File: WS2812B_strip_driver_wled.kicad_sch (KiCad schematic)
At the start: 114 parts, among them J1 CH_1, J2 CH_2, J3 CH_3, J4 CH_4, J5 PWR_IN, J6 uPhone, J8 USB_C_Receptacle_USB2.0_16P, K1 RELAY_1, K2 RELAY_2, K3 RELAY_3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

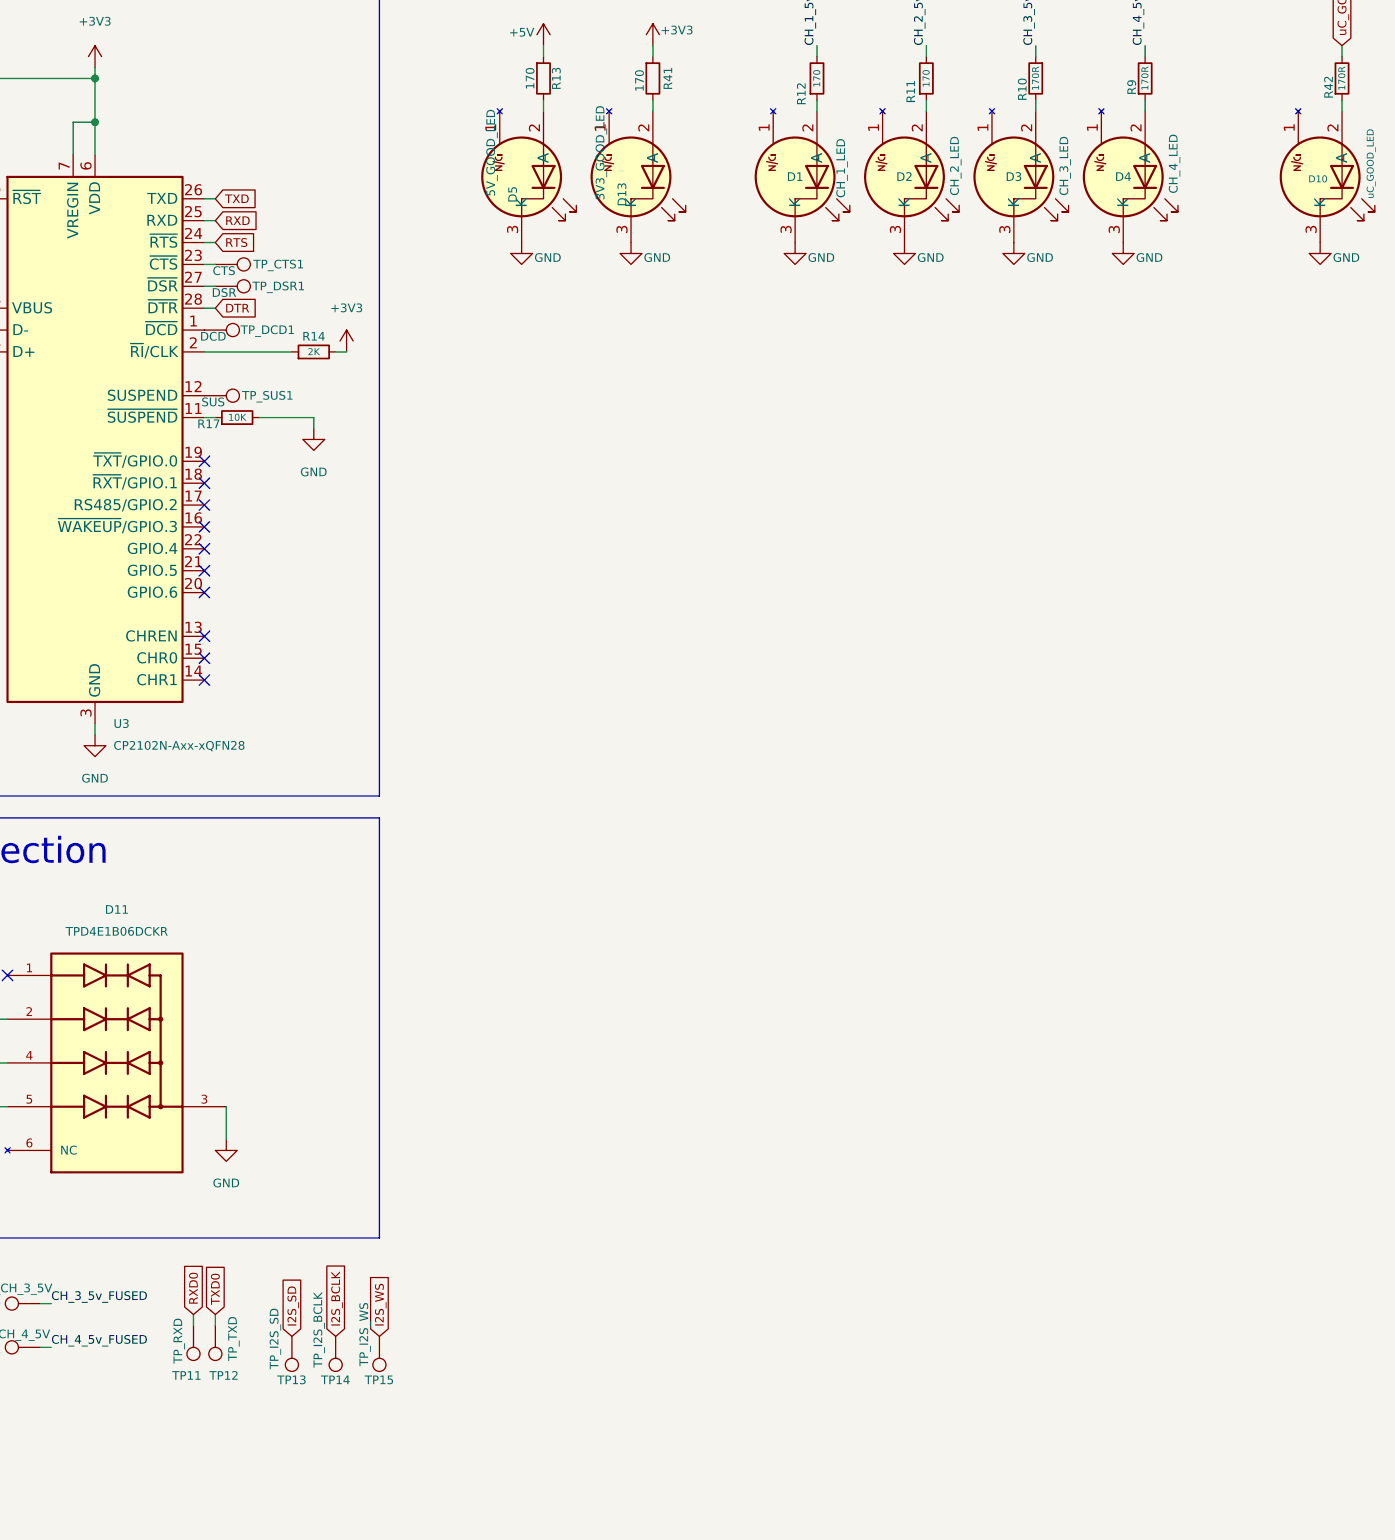
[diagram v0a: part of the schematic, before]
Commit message: More silkscreen improvements/additions
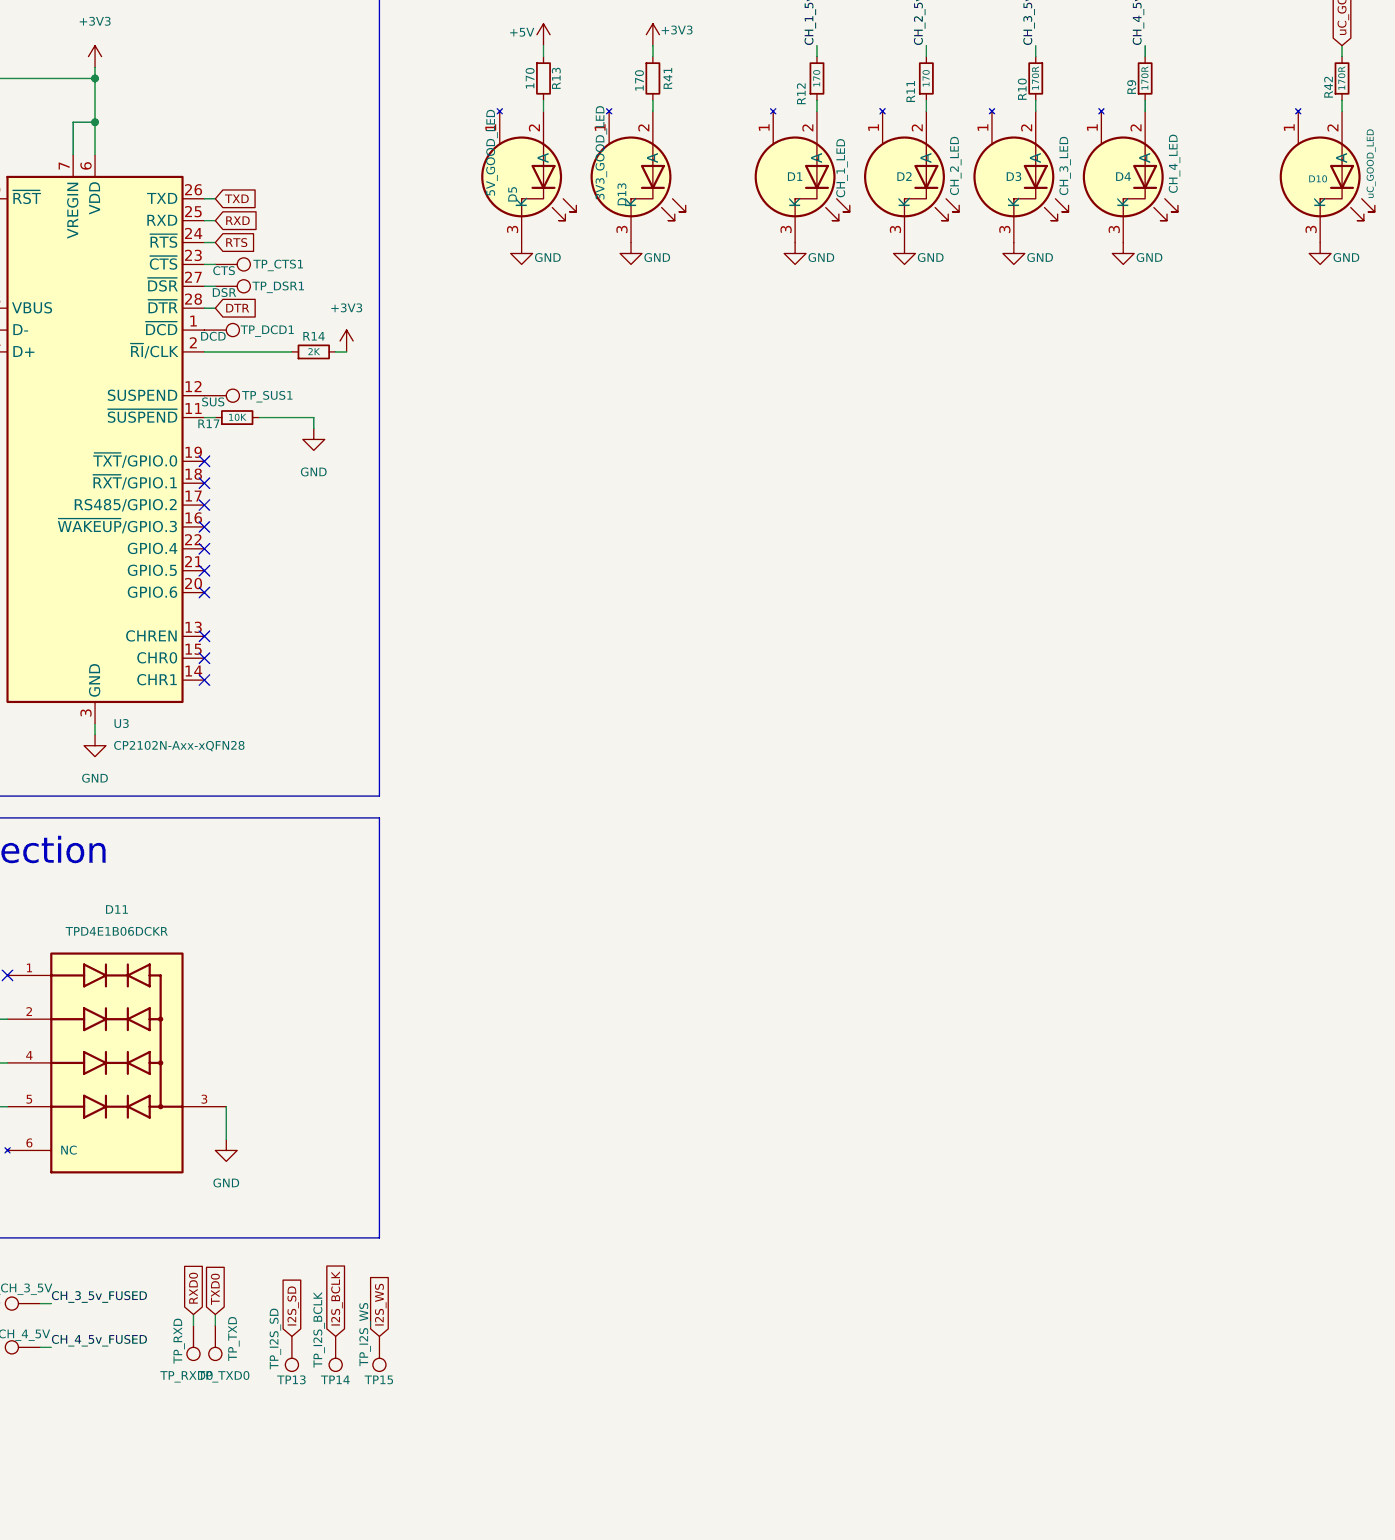
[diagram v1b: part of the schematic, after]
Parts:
- renumbered TP11 to TP_RXD0, TP12 to TP_TXD0
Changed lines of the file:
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@@
 			)
 		)
-		(property "Description" "Light emitting diode, small symbol, filled shape"
-			(at 331.47 40.64 0)
-			(effects
-				(font
-					(size 1.27 1.27)
-				)
-				(hide yes)
-			)
-		)
-		(property "Sim.Pins" "1=K 2=A"
+		(property "Description" ""
 			(at 331.47 40.64 0)
 			(effects
@@
 			)
 		)
-		(property "Description" "Light emitting diode, small symbol, filled shape"
-			(at 392.43 40.64 0)
-			(effects
-				(font
-					(size 1.27 1.27)
-				)
-				(hide yes)
-			)
-		)
-		(property "Sim.Pins" "1=K 2=A"
+		(property "Description" ""
 			(at 392.43 40.64 0)
 			(effects
@@
 		(on_board yes)
 		(dnp no)
-		(property "Reference" "TP12"
+		(property "Reference" "TP_TXD0"
 			(at 265.176 179.832 0)
 			(effects
@@
 			(project "WS2812B_strip_driver_wled"
 				(path "/a67e84d5-b812-4302-b0a6-200741099847"
-					(reference "TP12")
+					(reference "TP_TXD0")
 					(unit 1)
 				)
@@
 			)
 		)
-		(property "Description" "Light emitting diode, small symbol, filled shape"
-			(at 356.87 40.64 0)
-			(effects
-				(font
-					(size 1.27 1.27)
-				)
-				(hide yes)
-			)
-		)
-		(property "Sim.Pins" "1=K 2=A"
+		(property "Description" ""
 			(at 356.87 40.64 0)
 			(effects
@@
 			)
 		)
-		(property "Description" "Light emitting diode, small symbol, filled shape"
-			(at 344.17 40.64 0)
-			(effects
-				(font
-					(size 1.27 1.27)
-				)
-				(hide yes)
-			)
-		)
-		(property "Sim.Pins" "1=K 2=A"
+		(property "Description" ""
 			(at 344.17 40.64 0)
 			(effects
@@
 			)
 		)
-		(property "Description" "Light emitting diode, small symbol, filled shape"
-			(at 369.57 40.64 0)
-			(effects
-				(font
-					(size 1.27 1.27)
-				)
-				(hide yes)
-			)
-		)
-		(property "Sim.Pins" "1=K 2=A"
+		(property "Description" ""
 			(at 369.57 40.64 0)
 			(effects
@@
 			)
 		)
-		(property "Description" "Light emitting diode, small symbol, filled shape"
-			(at 312.42 40.64 0)
-			(effects
-				(font
-					(size 1.27 1.27)
-				)
-				(hide yes)
-			)
-		)
-		(property "Sim.Pins" "1=K 2=A"
+		(property "Description" ""
 			(at 312.42 40.64 0)
 			(effects
@@
 		(on_board yes)
 		(dnp no)
-		(property "Reference" "TP11"
+		(property "Reference" "TP_RXD0"
 			(at 260.858 179.832 0)
 			(effects
@@
 			(project "WS2812B_strip_driver_wled"
 				(path "/a67e84d5-b812-4302-b0a6-200741099847"
-					(reference "TP11")
+					(reference "TP_RXD0")
 					(unit 1)
 				)
@@
 			)
 		)
-		(property "Description" "Light emitting diode, small symbol, filled shape"
-			(at 299.72 40.64 0)
-			(effects
-				(font
-					(size 1.27 1.27)
-				)
-				(hide yes)
-			)
-		)
-		(property "Sim.Pins" "1=K 2=A"
+		(property "Description" ""
 			(at 299.72 40.64 0)
 			(effects
